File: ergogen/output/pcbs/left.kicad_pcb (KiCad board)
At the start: 2 copper layers, 137 x 110 mm, 79 parts

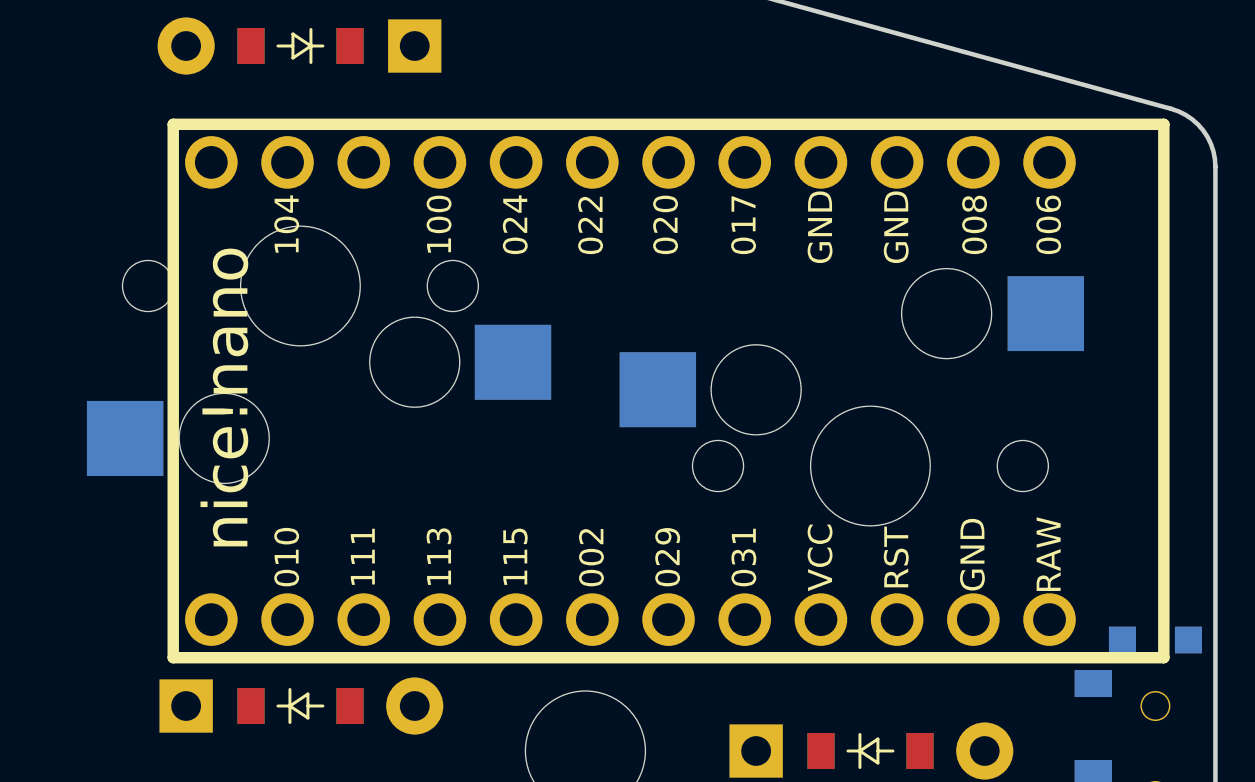
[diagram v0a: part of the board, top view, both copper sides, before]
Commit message: regenned with board flipped correctly; traced pcbs to be redone
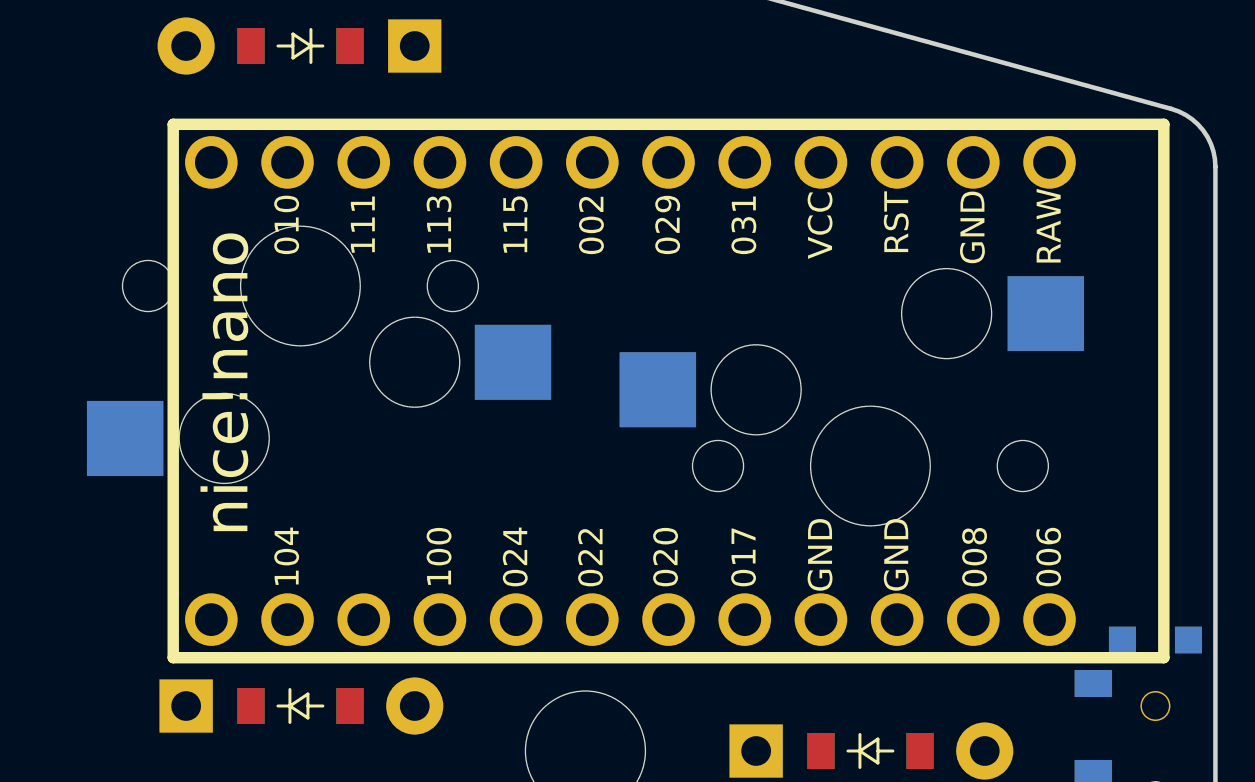
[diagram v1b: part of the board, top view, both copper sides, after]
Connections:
- D1 pad 1: P029 -> P020
- D10 pad 1: P031 -> P017
- D11 pad 1: P029 -> P020
- D12 pad 1: P002 -> P022
- D13 pad 1: P115 -> P024
- D14 pad 1: P113 -> P100
- D15 pad 1: P031 -> P017
- D16 pad 1: P029 -> P020
- D17 pad 1: P002 -> P022
- D18 pad 1: P115 -> P024
- D19 pad 1: P113 -> P100
- D2 pad 1: P002 -> P022
- D20 pad 1: P031 -> P017
- D21 pad 1: P029 -> P020
- D22 pad 1: P002 -> P022
- D23 pad 1: P115 -> P024
- D24 pad 1: P113 -> P100
- D25 pad 1: P031 -> P017
- D26 pad 1: P029 -> P020
- D27 pad 1: P002 -> P022
- D28 pad 1: P115 -> P024
- D29 pad 1: P029 -> P020
- D3 pad 1: P115 -> P024
- D30 pad 1: P002 -> P022
- D31 pad 1: P115 -> P024
- D32 pad 1: P113 -> P100
- D33 pad 1: P113 -> P100
- D34 pad 1: P031 -> P017
- D35 pad 1: P031 -> P017
- D4 pad 1: P113 -> P100
- D5 pad 1: P031 -> P017
- D6 pad 1: P029 -> P020
- D7 pad 1: P002 -> P022
- D8 pad 1: P115 -> P024
- D9 pad 1: P113 -> P100
- S1 pad 1: P024 -> P002
- S10 pad 1: P100 -> P115
- S11 pad 1: P011 -> P113
- S12 pad 1: P011 -> P113
- S13 pad 1: P011 -> P113
- S14 pad 1: P011 -> P113
- S15 pad 1: P011 -> P113
- S16 pad 1: P104 -> P111
- S17 pad 1: P104 -> P111
- S18 pad 1: P104 -> P111
- S19 pad 1: P104 -> P111
- S2 pad 1: P024 -> P002
- S20 pad 1: P104 -> P111
- S21 pad 1: P106 -> P010
- S22 pad 1: P106 -> P010
- S23 pad 1: P106 -> P010
- S24 pad 1: P106 -> P010
- S25 pad 1: P106 -> P010
- S26 pad 1: P020 -> P009
- S27 pad 1: P020 -> P009
- S28 pad 1: P020 -> P009
- S29 pad 1: P017 -> P031
- S3 pad 1: P024 -> P002
- S30 pad 1: P017 -> P031
- S31 pad 1: P017 -> P031
- S32 pad 1: P017 -> P031
- S33 pad 1: P017 -> P031
- S34 pad 1: P020 -> P009
- S35 pad 1: P020 -> P009
- S4 pad 1: P024 -> P002
- S5 pad 1: P024 -> P002
- S6 pad 1: P100 -> P115
- S7 pad 1: P100 -> P115
- S8 pad 1: P100 -> P115
- S9 pad 1: P100 -> P115

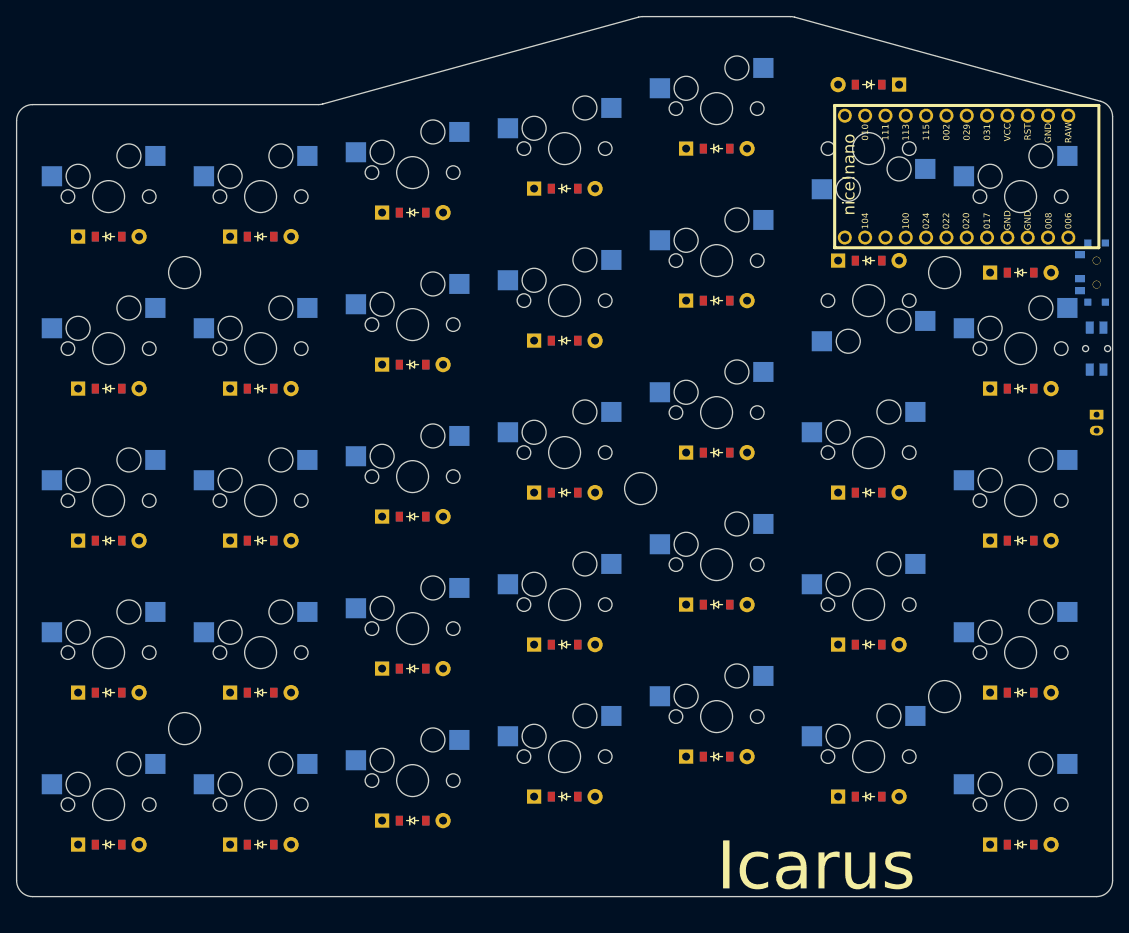
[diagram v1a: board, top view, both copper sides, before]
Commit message: regen board with custom footprints to have 3d models autogenned
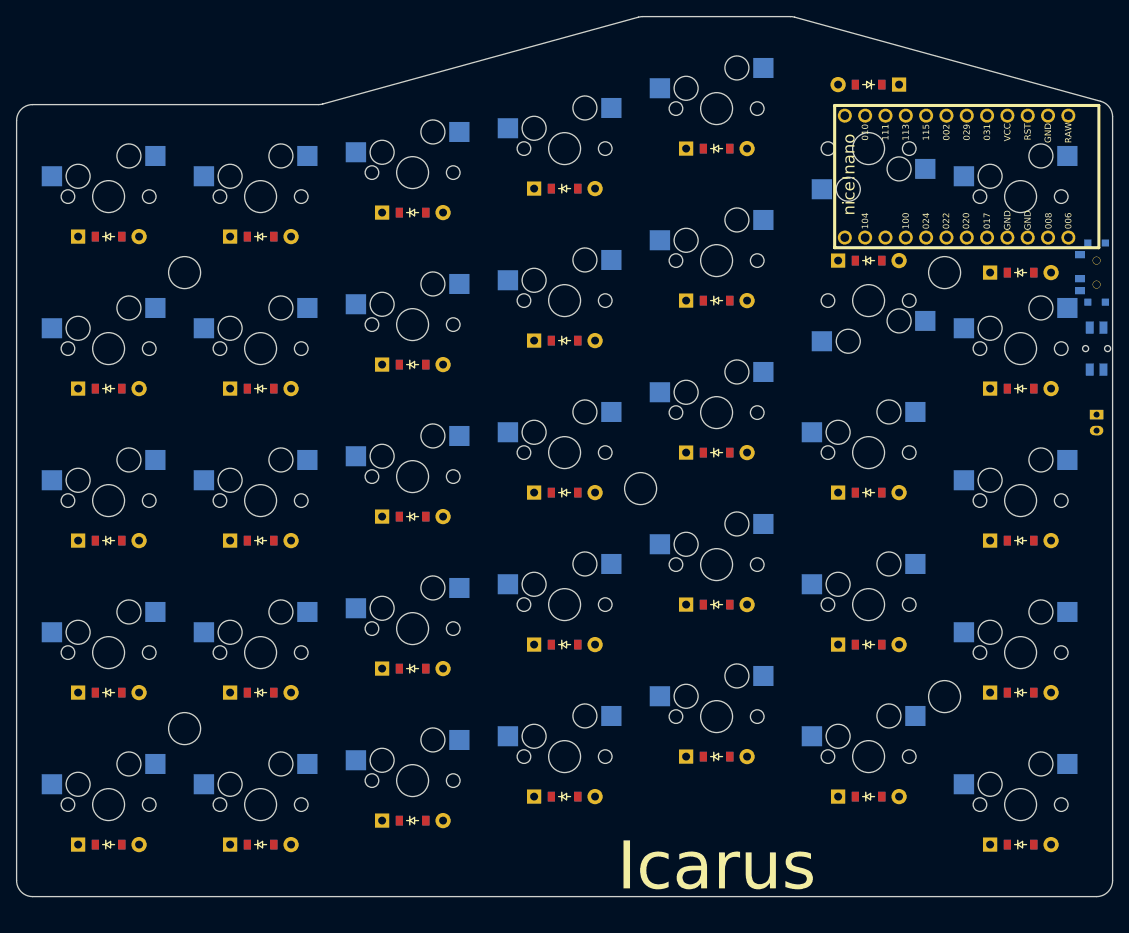
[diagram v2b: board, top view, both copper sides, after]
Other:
- net class Default removed
